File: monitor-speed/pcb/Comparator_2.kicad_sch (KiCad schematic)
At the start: 14 parts, among them K20 DIPxx-1Cxx-51x, Q2 BC848

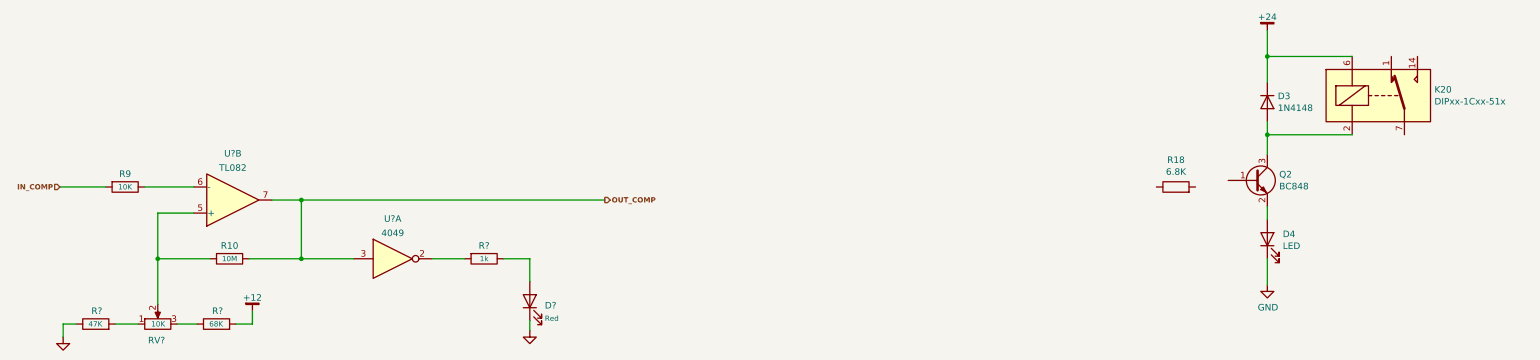
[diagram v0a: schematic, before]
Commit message: Monitor-Speed: New Schematic
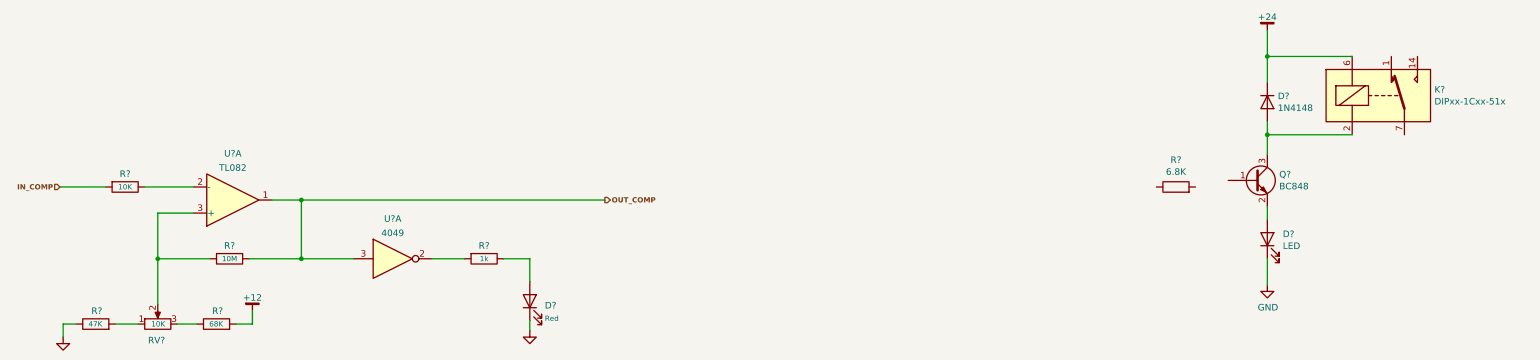
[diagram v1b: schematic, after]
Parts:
- renumbered D4 to D?, D3 to D?, K20 to K?, Q2 to Q?, R18 to R?, R9 to R?, R10 to R?
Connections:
- net OUT_COMP: now also U?.1; no longer U?.7
- net at R?.1: now also U?.2 (-); no longer U?.6 (-)
- net at R?.2, RV?.2: now also U?.3 (+); no longer U?.5 (+)
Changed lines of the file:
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@@
   (symbol (lib_id "Relay:DIPxx-1Cxx-51x") (at 353.06 71.12 0) (unit 1)
     (in_bom yes) (on_board yes)
-    (property "Reference" "K20" (id 0) (at 363.982 69.9516 0)
+    (property "Reference" "K?" (id 0) (at 363.982 69.9516 0)
       (effects (font (size 1.27 1.27)) (justify left))
     )
@@
   (symbol (lib_id "Device:R") (at 313.69 88.9 90) (unit 1)
     (in_bom yes) (on_board yes)
-    (property "Reference" "R18" (id 0) (at 313.69 83.6422 90))
+    (property "Reference" "R?" (id 0) (at 313.69 83.6422 90))
     (property "Value" "6.8K" (id 1) (at 313.69 85.9536 90))
     (property "Footprint" "Resistor_SMD:R_0603_1608Metric_Pad0.98x0.95mm_HandSolder" (id 2) (at 313.69 90.678 90)
@@
   (symbol (lib_id "Device:R") (at 109.22 88.9 270) (unit 1)
     (in_bom yes) (on_board yes)
-    (property "Reference" "R9" (id 0) (at 109.22 86.36 90))
+    (property "Reference" "R?" (id 0) (at 109.22 86.36 90))
     (property "Value" "10K" (id 1) (at 109.22 88.9 90)
       (effects (font (size 1.016 1.016)))
@@
   (symbol (lib_id "Device:R") (at 129.54 102.87 270) (unit 1)
     (in_bom yes) (on_board yes)
-    (property "Reference" "R10" (id 0) (at 129.54 100.33 90))
+    (property "Reference" "R?" (id 0) (at 129.54 100.33 90))
     (property "Value" "10M" (id 1) (at 129.54 102.87 90)
       (effects (font (size 1.016 1.016)))
@@
   (symbol (lib_id "Transistor_BJT:BC848") (at 328.93 87.63 0) (unit 1)
     (in_bom yes) (on_board yes)
-    (property "Reference" "Q2" (id 0) (at 333.7814 86.4616 0)
+    (property "Reference" "Q?" (id 0) (at 333.7814 86.4616 0)
       (effects (font (size 1.27 1.27)) (justify left))
     )
@@
   (symbol (lib_id "Device:LED") (at 331.47 99.06 90) (unit 1)
     (in_bom yes) (on_board yes)
-    (property "Reference" "D4" (id 0) (at 334.4672 98.0694 90)
+    (property "Reference" "D?" (id 0) (at 334.4672 98.0694 90)
       (effects (font (size 1.27 1.27)) (justify right))
     )
@@
   (symbol (lib_id "Diode:1N4148") (at 331.47 72.39 270) (unit 1)
     (in_bom yes) (on_board yes)
-    (property "Reference" "D3" (id 0) (at 333.502 71.2216 90)
+    (property "Reference" "D?" (id 0) (at 333.502 71.2216 90)
       (effects (font (size 1.27 1.27)) (justify left))
     )
@@
     (pin "1")
   )
-  (symbol (lib_id "Amplifier_Operational:TL082") (at 130.175 91.44 0) (mirror x) (unit 2)
+  (symbol (lib_id "Amplifier_Operational:TL082") (at 130.175 91.44 0) (mirror x) (unit 1)
     (in_bom yes) (on_board yes) (fields_autoplaced)
     (property "Reference" "U?" (id 0) (at 130.175 82.3935 0))
@@
       (effects (font (size 1.27 1.27)) hide)
     )
-    (pin "5")
-    (pin "6")
-    (pin "7")
+    (pin "1")
+    (pin "2")
+    (pin "3")
   )
   (symbol (lib_id "Device:R") (at 179.07 102.87 270) (unit 1)

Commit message: Monitor-Speed: Add Relay Circuit
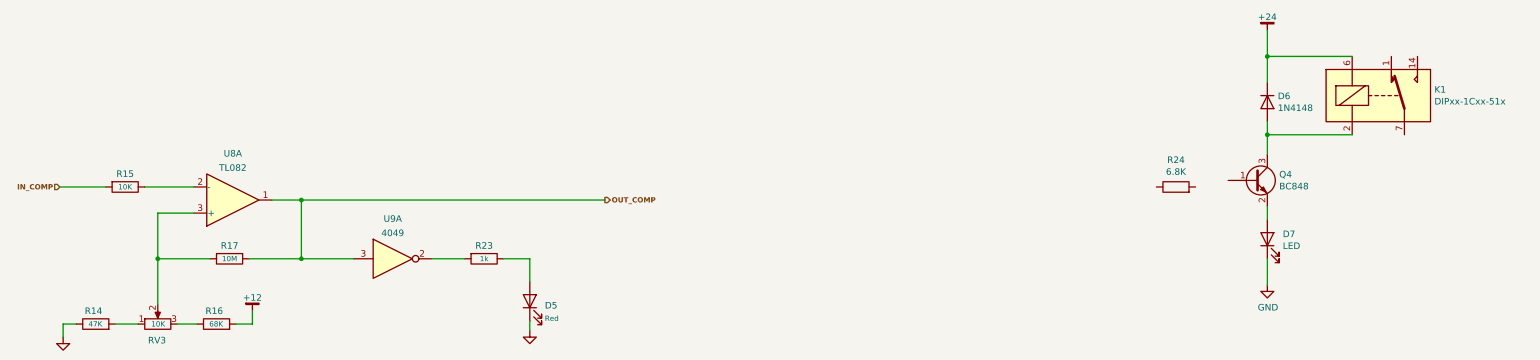
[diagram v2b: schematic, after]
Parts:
- gave numbers to parts that had none: 14
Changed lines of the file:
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@@
   (symbol (lib_id "Relay:DIPxx-1Cxx-51x") (at 353.06 71.12 0) (unit 1)
     (in_bom yes) (on_board yes)
-    (property "Reference" "K?" (id 0) (at 363.982 69.9516 0)
+    (property "Reference" "K1" (id 0) (at 363.982 69.9516 0)
       (effects (font (size 1.27 1.27)) (justify left))
     )
@@
   (symbol (lib_id "Device:R") (at 313.69 88.9 90) (unit 1)
     (in_bom yes) (on_board yes)
-    (property "Reference" "R?" (id 0) (at 313.69 83.6422 90))
+    (property "Reference" "R24" (id 0) (at 313.69 83.6422 90))
     (property "Value" "6.8K" (id 1) (at 313.69 85.9536 90))
     (property "Footprint" "Resistor_SMD:R_0603_1608Metric_Pad0.98x0.95mm_HandSolder" (id 2) (at 313.69 90.678 90)
@@
   (symbol (lib_id "Device:R") (at 109.22 88.9 270) (unit 1)
     (in_bom yes) (on_board yes)
-    (property "Reference" "R?" (id 0) (at 109.22 86.36 90))
+    (property "Reference" "R15" (id 0) (at 109.22 86.36 90))
     (property "Value" "10K" (id 1) (at 109.22 88.9 90)
       (effects (font (size 1.016 1.016)))
@@
   (symbol (lib_id "Device:R") (at 129.54 102.87 270) (unit 1)
     (in_bom yes) (on_board yes)
-    (property "Reference" "R?" (id 0) (at 129.54 100.33 90))
+    (property "Reference" "R17" (id 0) (at 129.54 100.33 90))
     (property "Value" "10M" (id 1) (at 129.54 102.87 90)
       (effects (font (size 1.016 1.016)))
@@
   (symbol (lib_id "Transistor_BJT:BC848") (at 328.93 87.63 0) (unit 1)
     (in_bom yes) (on_board yes)
-    (property "Reference" "Q?" (id 0) (at 333.7814 86.4616 0)
+    (property "Reference" "Q4" (id 0) (at 333.7814 86.4616 0)
       (effects (font (size 1.27 1.27)) (justify left))
     )
@@
   (symbol (lib_id "Device:LED") (at 331.47 99.06 90) (unit 1)
     (in_bom yes) (on_board yes)
-    (property "Reference" "D?" (id 0) (at 334.4672 98.0694 90)
+    (property "Reference" "D7" (id 0) (at 334.4672 98.0694 90)
       (effects (font (size 1.27 1.27)) (justify right))
     )
@@
   (symbol (lib_id "power:GND") (at 331.47 107.95 0) (unit 1)
     (in_bom yes) (on_board yes)
-    (property "Reference" "#PWR?" (id 0) (at 331.47 114.3 0)
+    (property "Reference" "#PWR029" (id 0) (at 331.47 114.3 0)
       (effects (font (size 1.27 1.27)) hide)
     )
@@
   (symbol (lib_id "Diode:1N4148") (at 331.47 72.39 270) (unit 1)
     (in_bom yes) (on_board yes)
-    (property "Reference" "D?" (id 0) (at 333.502 71.2216 90)
+    (property "Reference" "D6" (id 0) (at 333.502 71.2216 90)
       (effects (font (size 1.27 1.27)) (justify left))
     )
@@
   (symbol (lib_id "4xxx:4049") (at 161.29 102.87 0) (unit 1)
     (in_bom yes) (on_board yes) (fields_autoplaced)
-    (property "Reference" "U?" (id 0) (at 161.29 95.0935 0))
+    (property "Reference" "U9" (id 0) (at 161.29 95.0935 0))
     (property "Value" "4049" (id 1) (at 161.29 97.8686 0))
     (property "Footprint" "" (id 2) (at 161.29 102.87 0)
@@
   (symbol (lib_id "power:GND") (at 97.155 118.11 0) (unit 1)
     (in_bom yes) (on_board yes)
-    (property "Reference" "#PWR?" (id 0) (at 97.155 124.46 0)
+    (property "Reference" "#PWR025" (id 0) (at 97.155 124.46 0)
       (effects (font (size 1.27 1.27)) hide)
     )
@@
   (symbol (lib_id "Device:R_POT") (at 115.57 115.57 90) (unit 1)
     (in_bom yes) (on_board yes)
-    (property "Reference" "RV?" (id 0) (at 113.665 118.745 90)
+    (property "Reference" "RV3" (id 0) (at 113.665 118.745 90)
       (effects (font (size 1.27 1.27)) (justify right))
     )
@@
   (symbol (lib_name "LED_1") (lib_id "Device:LED") (at 187.96 111.125 90) (unit 1)
     (in_bom yes) (on_board yes) (fields_autoplaced)
-    (property "Reference" "D?" (id 0) (at 190.881 111.9603 90)
+    (property "Reference" "D5" (id 0) (at 190.881 111.9603 90)
       (effects (font (size 1.27 1.27)) (justify right))
     )
@@
   (symbol (lib_id "Device:R") (at 103.505 115.57 90) (unit 1)
     (in_bom yes) (on_board yes)
-    (property "Reference" "R?" (id 0) (at 104.775 113.03 90)
+    (property "Reference" "R14" (id 0) (at 104.775 113.03 90)
       (effects (font (size 1.27 1.27)) (justify left))
     )
@@
   (symbol (lib_id "Device:R") (at 127 115.57 90) (unit 1)
     (in_bom yes) (on_board yes)
-    (property "Reference" "R?" (id 0) (at 128.27 113.03 90)
+    (property "Reference" "R16" (id 0) (at 128.27 113.03 90)
       (effects (font (size 1.27 1.27)) (justify left))
     )
@@
   (symbol (lib_id "power1:+24") (at 331.47 58.42 0) (unit 1)
     (in_bom yes) (on_board yes) (fields_autoplaced)
-    (property "Reference" "#PWR?" (id 0) (at 331.47 57.15 0)
+    (property "Reference" "#PWR028" (id 0) (at 331.47 57.15 0)
       (effects (font (size 0.762 0.762)) hide)
     )
@@
   (symbol (lib_id "power1:+12") (at 133.985 113.03 0) (unit 1)
     (in_bom yes) (on_board yes)
-    (property "Reference" "#PWR?" (id 0) (at 133.985 111.76 0)
+    (property "Reference" "#PWR026" (id 0) (at 133.985 111.76 0)
       (effects (font (size 0.762 0.762)) hide)
     )
@@
   (symbol (lib_id "Amplifier_Operational:TL082") (at 130.175 91.44 0) (mirror x) (unit 1)
     (in_bom yes) (on_board yes) (fields_autoplaced)
-    (property "Reference" "U?" (id 0) (at 130.175 82.3935 0))
+    (property "Reference" "U8" (id 0) (at 130.175 82.3935 0))
     (property "Value" "TL082" (id 1) (at 130.175 85.1686 0))
     (property "Footprint" "" (id 2) (at 130.175 91.44 0)
@@
   (symbol (lib_id "Device:R") (at 179.07 102.87 270) (unit 1)
     (in_bom yes) (on_board yes)
-    (property "Reference" "R?" (id 0) (at 179.07 100.33 90))
+    (property "Reference" "R23" (id 0) (at 179.07 100.33 90))
     (property "Value" "1k" (id 1) (at 179.07 102.87 90)
       (effects (font (size 1.016 1.016)))
@@
   (symbol (lib_id "power:GND") (at 187.96 116.84 0) (unit 1)
     (in_bom yes) (on_board yes)
-    (property "Reference" "#PWR?" (id 0) (at 187.96 123.19 0)
-      (effects (font (size 1.27 1.27)) hide)
-    )
+    (property "Reference" "#PWR027" (id 0) (at 187.96 123.19 0)
+      (effects (font (size 1.27 1.27)) hide)
+    )
